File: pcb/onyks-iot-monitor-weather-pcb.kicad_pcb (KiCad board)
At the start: 2 copper layers, 100 x 100 mm, 42 parts, among them J1 53398-0371, J10 Conn_01x06_Pin, J13 Conn_01x02_Pin, J14 Conn_02x05_Odd_Even, J2 53398-0371, J3 Conn_01x04_Pin, J4 53398-0371, J5 53398-0371, J6 53398-0371, J7 53398-0371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

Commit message: PCB poprawione
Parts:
- moved J10 58.0 mm to (78.6, 51.6), turned to 90 degrees
- moved J6 33.2 mm to (103.8, 72.6), turned to 90 degrees
- moved R10 33.0 mm to (101.2, 65.6)
- moved R5 33.0 mm to (105.2, 65.6)
- moved R7 28.4 mm to (103.2, 63.8)
- moved R12 28.3 mm to (99.2, 63.8)
- moved J5 24.9 mm to (97.8, 72.6), turned to 90 degrees
- moved J3 24.4 mm to (129.6, 66.9), turned to -90 degrees
- moved R11 24.2 mm to (97.2, 62.0)
- moved R6 24.2 mm to (101.2, 62.0)
- moved R13 19.1 mm to (95.2, 60.2)
- moved R8 19.1 mm to (99.2, 60.2)
- moved J4 16.3 mm to (91.4, 72.6), turned to 90 degrees
- moved R4 13.9 mm to (93.2, 58.4)
- moved R9 13.9 mm to (97.2, 58.4)
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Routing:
- net +3.3V: track 312.7 -> 214.6 mm, vias 6 -> 7
- net VCC: track 305.4 -> 230.0 mm, vias 2 -> 6
- net /ESP32/EN: track 118.4 -> 185.7 mm, vias 3 -> 4
- net /ESP32/UART_PROGRAM_RXD: track 77.0 -> 138.2 mm
- net /ESP32/IO35: track 83.1 -> 142.1 mm
- net /ESP32/UART_PROGRAM_TXD: track 82.0 -> 139.2 mm, vias 2 -> 3
- net /ESP32/IO27: track 52.9 -> 17.5 mm
- net /ESP32/IO22: track 61.1 -> 27.4 mm
- net /ESP32/IO26: track 48.2 -> 17.4 mm
- net /ESP32/IO25: track 44.2 -> 18.9 mm
- net /ESP32/IO33: track 39.1 -> 20.2 mm
- net /ESP32/MTDO: track 23.8 -> 10.0 mm
- net /ESP32/IO32: track 33.8 -> 22.0 mm
- net Net-(J7-Pin_3): track 8.50 -> 19.4 mm
- net /ESP32/IO0: track 34.6 -> 23.7 mm
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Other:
- board size 100 x 100 mm -> 100 x 52.4 mm

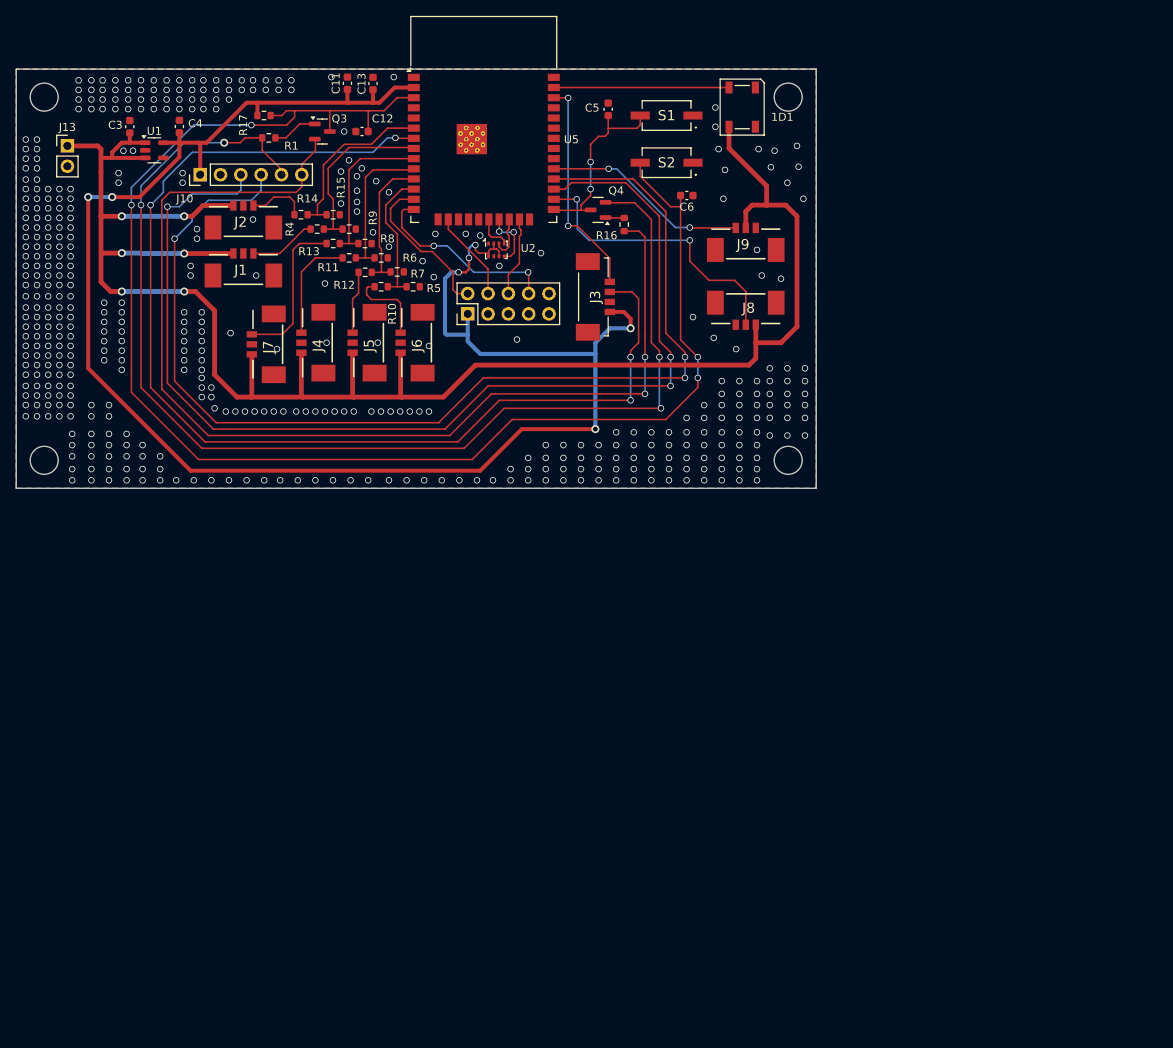
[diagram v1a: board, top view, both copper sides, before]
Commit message: PCB jeszcze mniejsza wersja
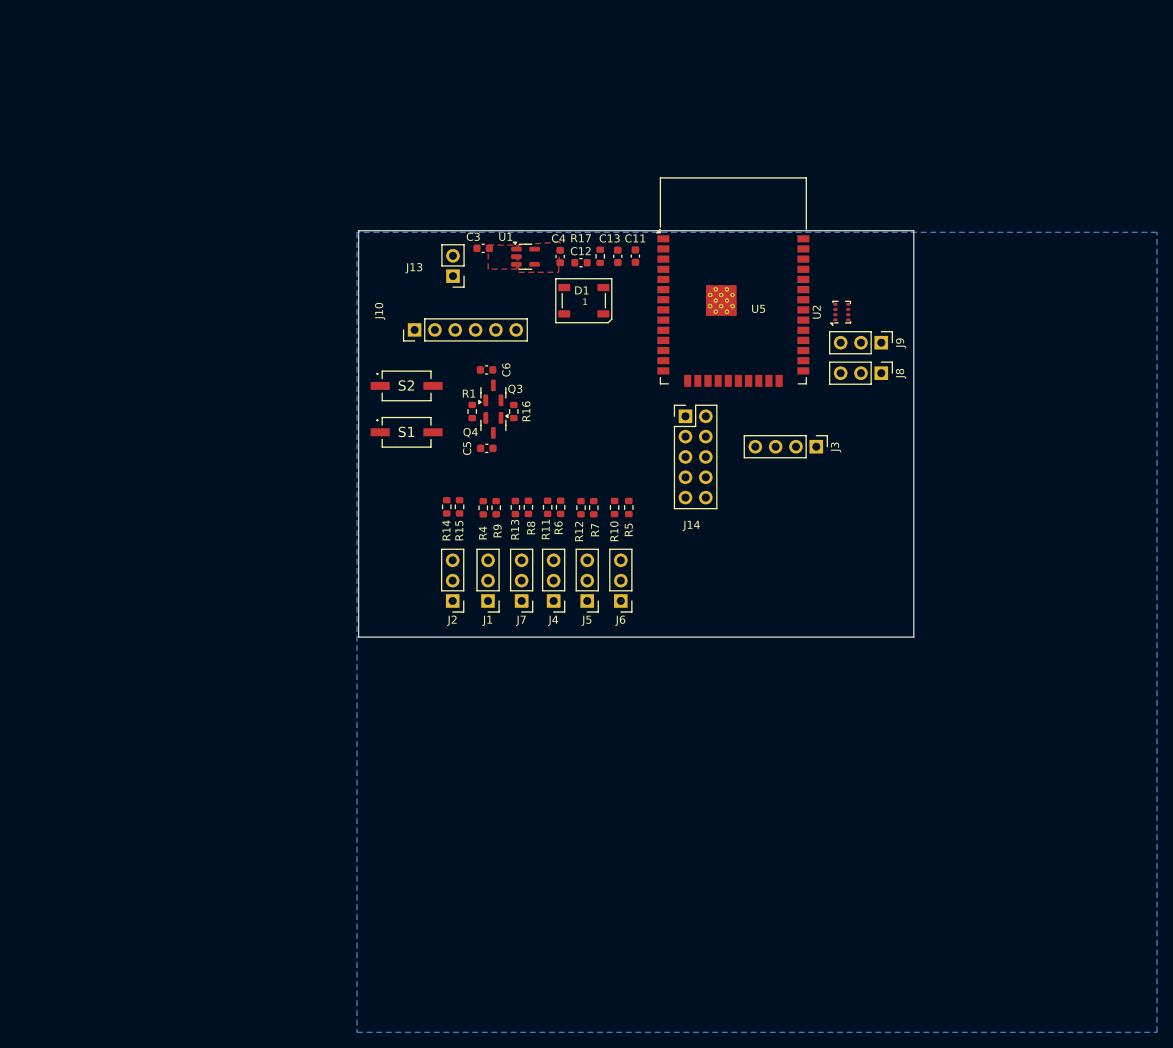
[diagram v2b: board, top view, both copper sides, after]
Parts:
- J1, J2, J4, J5, J6, J7, J8, J9: footprint 1bmoje:53398-0371 -> Connector_PinHeader_2.54mm:PinHeader_1x03_P2.54mm_Vertical
- J3: footprint 1bmoje:533980471- MOLEXx4 -> Connector_PinHeader_2.54mm:PinHeader_1x04_P2.54mm_Vertical
- moved J2 55.8 mm to (110.2, 104.9), turned to 180 degrees
- moved J1 53.0 mm to (114.6, 104.9), turned to 180 degrees
- moved S1 51.2 mm to (104.4, 83.8), turned to 0 degrees
- moved J13 50.9 mm to (110.2, 64.3), turned to 180 degrees
- moved C4 50.3 mm to (123.6, 61.8), turned to -90 degrees
- moved U1 48.3 mm to (119.3, 61.9)
- moved C3 46.7 mm to (114.0, 60.8), turned to 180 degrees
- moved J7 46.4 mm to (118.8, 104.9), turned to 180 degrees
- moved R17 45.6 mm to (128.6, 61.8), turned to -90 degrees
- moved J4 45.0 mm to (122.8, 104.9), turned to 180 degrees
- moved C5 45.0 mm to (114.4, 85.8), turned to 0 degrees
- moved U2 43.9 mm to (158.8, 68.8), turned to 90 degrees
- moved J5 43.5 mm to (127.0, 104.9), turned to 180 degrees
- moved S2 42.8 mm to (104.4, 78.0), turned to 0 degrees
- moved R1 42.6 mm to (112.6, 81.2), turned to 90 degrees
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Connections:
- J3 pad 2: /ESP32/IO35 -> /ESP32/IO2
- J8 pad 2: /ESP32/IO4 -> GND
- J8 pad 3: GND -> /ESP32/IO4
- J9 pad 1: /ESP32/IO5 -> VCC
- J9 pad 2: VCC -> GND
- J9 pad 3: GND -> /ESP32/IO5
- R14 pad 2: /ESP32/IO34 -> /ESP32/IO35
- R15 pad 1: /ESP32/IO34 -> /ESP32/IO35
- U5 pad 20: /ESP32/SCK -> unconnected-(U5-SCK/CLK-Pad20)
- U5 pad 21: /ESP32/SDO -> unconnected-(U5-SDO/SD0-Pad21)
- U5 pad 22: /ESP32/SDI -> unconnected-(U5-SDI/SD1-Pad22)
- U5 pad 24: unconnected-(U5-IO2-Pad24) -> /ESP32/IO2
- U5 pad 27: /ESP32/UART_PROGRAM_RXD -> unconnected-(U5-IO16-Pad27)
- U5 pad 28: /ESP32/UART_PROGRAM_TXD -> unconnected-(U5-IO17-Pad28)
- U5 pad 30: unconnected-(U5-IO18-Pad30) -> /ESP32/SDI
- U5 pad 31: unconnected-(U5-IO19-Pad31) -> /ESP32/SCK
- U5 pad 33: unconnected-(U5-IO21-Pad33) -> /ESP32/SDO
- U5 pad 34: unconnected-(U5-RXD0/IO3-Pad34) -> /ESP32/UART_PROGRAM_RXD
- U5 pad 35: unconnected-(U5-TXD0/IO1-Pad35) -> /ESP32/UART_PROGRAM_TXD
- U5 pad 37: /ESP32/LED -> unconnected-(U5-IO23-Pad37)
- U5 pad 6: /ESP32/IO34 -> /ESP32/LED
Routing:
- net VCC: track 230.0 -> 0.00 mm, vias 6 -> 0
- net +3.3V: track 214.6 -> 0.00 mm, vias 7 -> 0
- net /ESP32/EN: track 185.7 -> 0.00 mm, vias 4 -> 0
- net /ESP32/UART_PROGRAM_DTR: track 149.3 -> 0.00 mm, vias 4 -> 0
- net /ESP32/IO35: track 142.1 -> 0.00 mm, vias 4 -> 0
- net /ESP32/UART_PROGRAM_TXD: track 139.2 -> 0.00 mm, vias 3 -> 0
- net /ESP32/UART_PROGRAM_RXD: track 138.2 -> 0.00 mm, vias 3 -> 0
- net /ESP32/UART_PROGRAM_RTS: track 135.8 -> 0.00 mm, vias 2 -> 0
- net /ESP32/IO4: track 36.9 -> 0.00 mm, vias 2 -> 0
- net /ESP32/IO22: track 27.4 -> 0.00 mm, vias 2 -> 0
- net /ESP32/IO5: track 25.7 -> 0.00 mm, vias 2 -> 0
- net /ESP32/MTDI: track 24.5 -> 0.00 mm, vias 2 -> 0
- net /ESP32/IO0: track 23.7 -> 0.00 mm, vias 2 -> 0
- net /ESP32/IO34: track 22.1 -> 0.00 mm
- net /ESP32/LED: track 22.0 -> 0.00 mm
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- added copper zone on F.Cu, net VCC
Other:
- board size 100 x 52.4 mm -> 69.4 x 50.8 mm

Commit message: 4 layer PCB
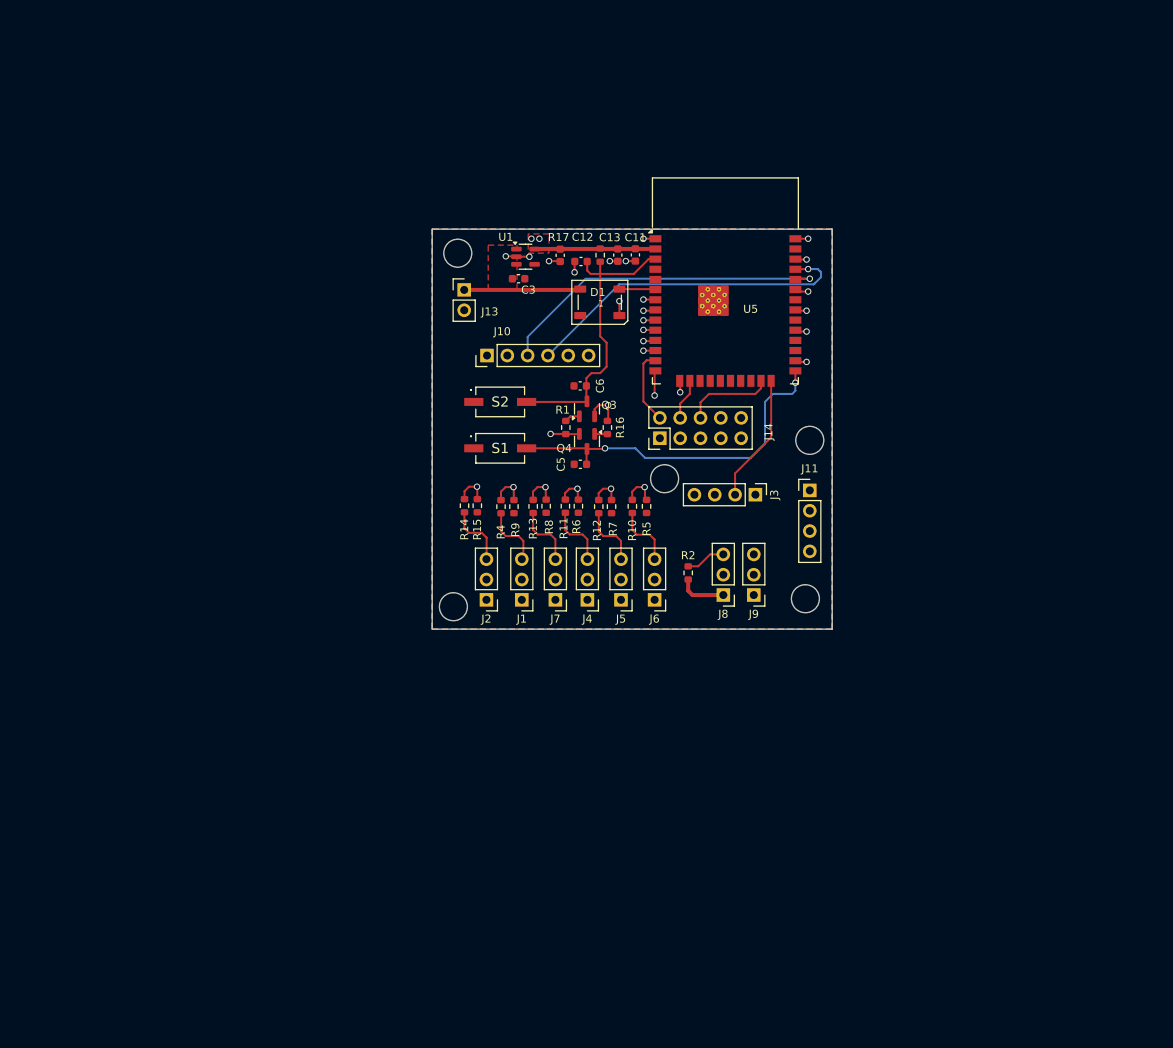
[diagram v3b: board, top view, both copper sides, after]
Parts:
- removed U2: BMP280, Package_LGA:Bosch_LGA-8_2x2.5mm_P0.65mm_ClockwisePinNumbering
- added J11: Conn_01x04_Pin, Connector_PinHeader_2.54mm:PinHeader_1x04_P2.54mm_Vertical, F.Cu at (154.8, 91.1)
- added R2: 10k, Resistor_SMD:R_0603_1608Metric, F.Cu at (139.6, 101.4)
- moved J9 35.3 mm to (147.8, 104.1), turned to 180 degrees
- moved J8 34.0 mm to (144.0, 104.1), turned to 180 degrees
- moved C5 11.9 mm to (126.1, 87.8)
- moved Q3 11.9 mm to (127.0, 80.9)
- moved Q4 11.9 mm to (127.0, 84.9)
- moved R1 11.9 mm to (124.3, 83.2)
- moved R16 11.9 mm to (129.5, 83.2)
- moved C6 11.9 mm to (126.1, 78.0)
- moved S1 11.9 mm to (116.1, 85.8)
- moved S2 11.9 mm to (116.1, 80.0)
- moved J3 9.69 mm to (148.0, 91.6)
- moved J10 9.60 mm to (114.5, 74.2)
- moved C3 5.83 mm to (118.4, 64.6), turned to 0 degrees
- moved J1 4.22 mm to (118.8, 104.7)
- moved J2 4.22 mm to (114.4, 104.7)
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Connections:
- U5 pad 30: /ESP32/SDI -> unconnected-(U5-IO18-Pad30)
- U5 pad 31: /ESP32/SCK -> /ESP32/SCL
- U5 pad 33: /ESP32/SDO -> /ESP32/SDA
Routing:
- net /ESP32/IO35: track 0.00 -> 46.5 mm, vias 0 -> 2
- net /ESP32/IO0: track 0.00 -> 45.1 mm, vias 0 -> 2
- net /ESP32/UART_PROGRAM_RXD: track 0.00 -> 42.4 mm, vias 0 -> 1
- net /ESP32/UART_PROGRAM_TXD: track 0.00 -> 42.4 mm, vias 0 -> 1
- net /ESP32/IO32: track 0.00 -> 40.9 mm, vias 0 -> 2
- net /ESP32/IO4: track 0.00 -> 39.1 mm, vias 0 -> 1
- net /ESP32/EN: track 0.00 -> 37.7 mm
- net /ESP32/SCL: track 0.00 -> 36.8 mm, vias 0 -> 1
- net /ESP32/IO33: track 0.00 -> 36.2 mm, vias 0 -> 2
- net /ESP32/SDA: track 0.00 -> 35.9 mm, vias 0 -> 1
- net /ESP32/IO22: track 0.00 -> 34.9 mm, vias 0 -> 1
- net /ESP32/IO5: track 0.00 -> 33.6 mm, vias 0 -> 1
- net /ESP32/IO25: track 0.00 -> 31.4 mm, vias 0 -> 2
- net /ESP32/IO26: track 0.00 -> 26.7 mm, vias 0 -> 2
- net /ESP32/IO27: track 0.00 -> 23.0 mm, vias 0 -> 2
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- added copper zone on F.Cu, net +3.3V
- added copper zone on In2.Cu, net +3.3V
- added copper zone on In1.Cu, net GND
- added copper zone on In2.Cu, net VCC
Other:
- board size 69.4 x 50.8 mm -> 50 x 50 mm
- copper layers 2 -> 4

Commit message: gerbery dodane do folderu fabrication
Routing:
- net /ESP32/SDA: track 35.9 -> 36.9 mm
- net /ESP32/UART_PROGRAM_TXD: track 42.4 -> 43.1 mm
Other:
- outline, holes or cut-outs redrawn
